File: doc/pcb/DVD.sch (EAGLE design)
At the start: 26 parts, among them IC1 7805, IC2 74HC14N

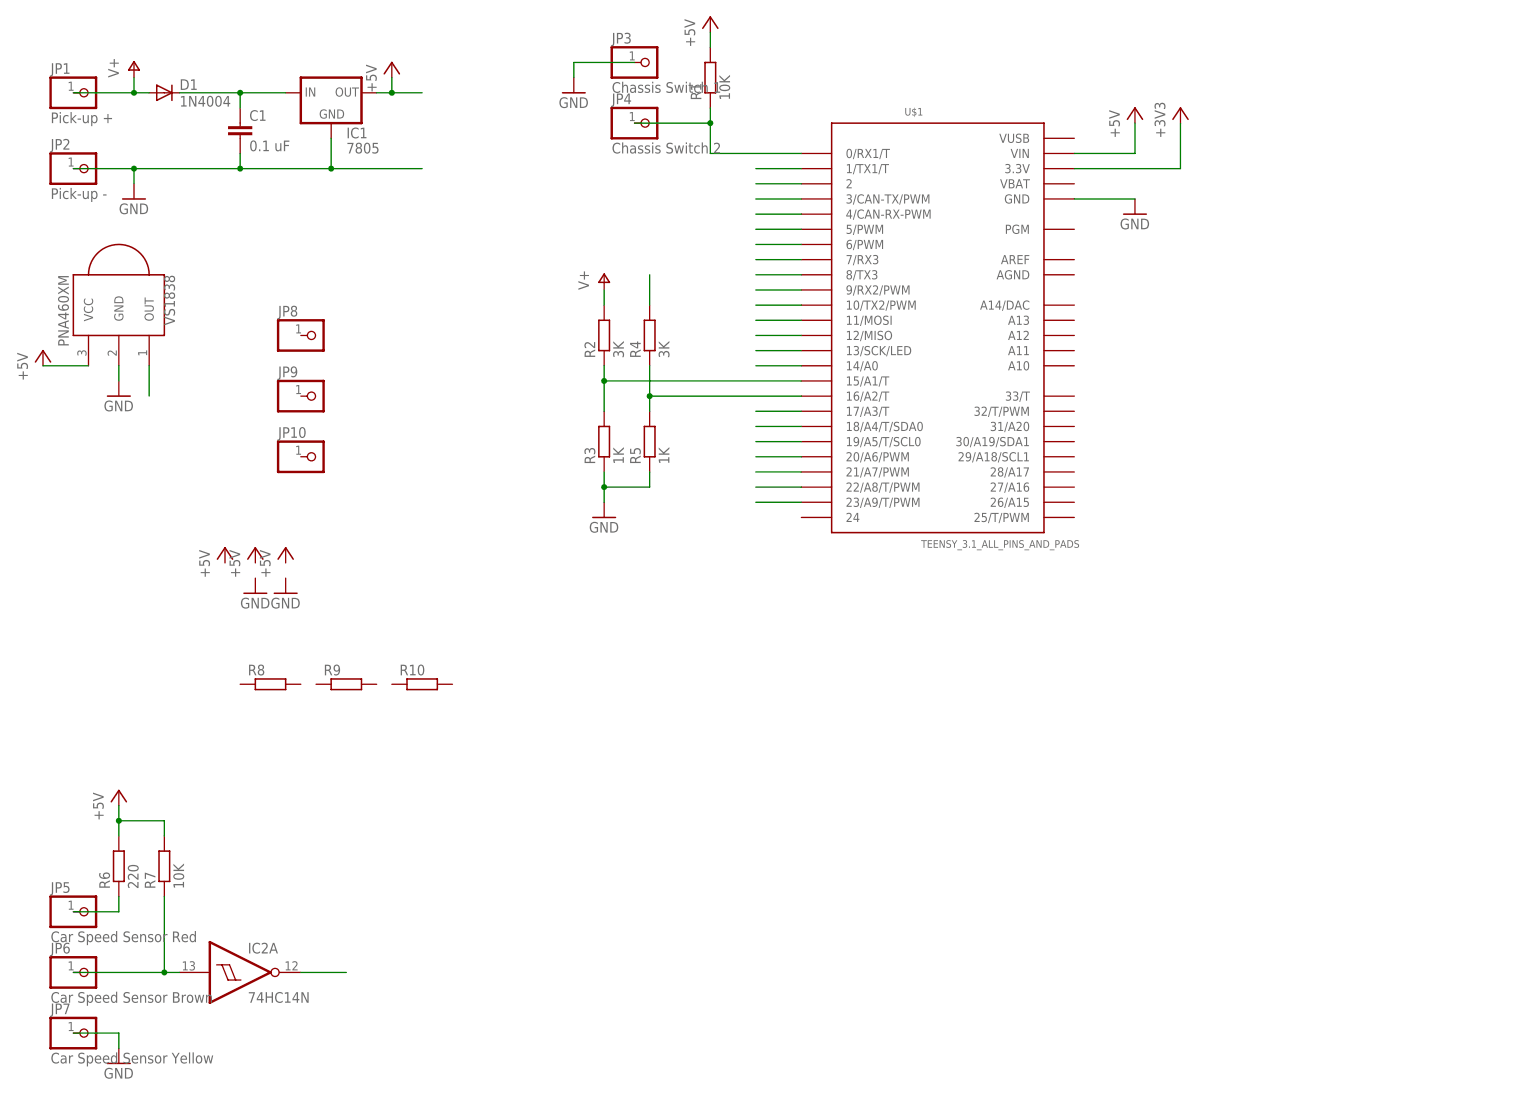
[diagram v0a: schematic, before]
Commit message: PCB Schematics update
Added all known components
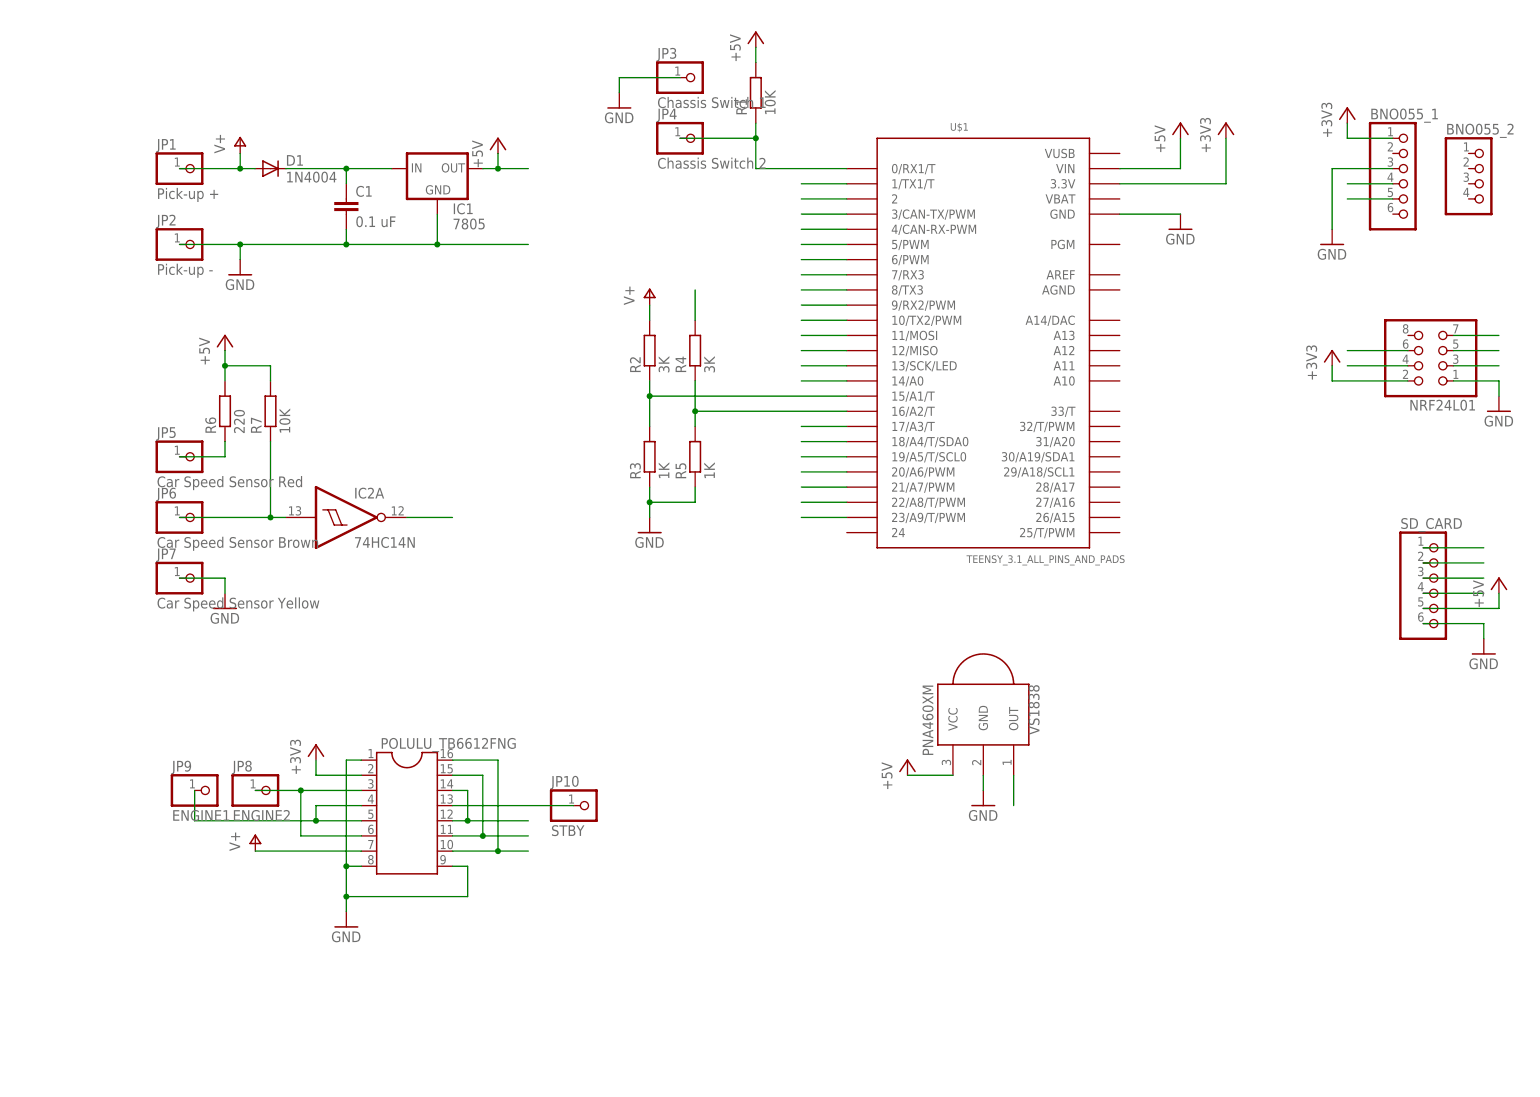
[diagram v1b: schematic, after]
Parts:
- removed R10, R8, R9: (no value), resistor:R-EU_0204/7
- added BNO055_1, SD_CARD: (no value), adafruit:PINHD-1X6
- added BNO055_2: (no value), pinhead:PINHD-1X4
- added NRF24L01: (no value), adafruit:PINHD-2X4
- added POLULU_TB6612FNG: (no value), ic-package:DIL16
- JP10: value (none) -> STBY
- JP8: value (none) -> ENGINE2
- JP9: value (none) -> ENGINE1
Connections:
- removed net N$12: U$1.18/A4/T/SDA0
- removed net N$13: U$1.19/A5/T/SCL0
- removed net N$14: U$1.21/A7/PWM
- removed net N$15: U$1.22/A8/T/PWM
- removed net N$16: U$1.23/A9/T/PWM
- removed net N$23: U$1.14/A0
- removed net N$5: U$1.9/RX2/PWM
- removed net N$6: U$1.10/TX2/PWM
- removed net N$7: U$1.11/MOSI
- removed net N$8: U$1.12/MISO
- new net CE: NRF24L01.3, U$1.8/TX3
- new net CSN_RADIO: NRF24L01.4, U$1.10/TX2/PWM
- new net CSN_SD: SD_CARD.1, U$1.9/RX2/PWM
- new net ENGINE1: JP9.1, POLULU_TB6612FNG.4, POLULU_TB6612FNG.5
- new net IN1: POLULU_TB6612FNG.12, POLULU_TB6612FNG.14, U$1.23/A9/T/PWM
- new net IN2: POLULU_TB6612FNG.11, POLULU_TB6612FNG.15, U$1.22/A8/T/PWM
- new net JP8: JP8.1, POLULU_TB6612FNG.3, POLULU_TB6612FNG.6
- new net MISO: NRF24L01.7, SD_CARD.4, U$1.12/MISO
- new net MOSI: NRF24L01.6, SD_CARD.3, U$1.11/MOSI
- new net PWM: POLULU_TB6612FNG.10, POLULU_TB6612FNG.16, U$1.21/A7/PWM
- new net SCK: NRF24L01.5, SD_CARD.2, U$1.14/A0
- new net SCL: BNO055_1.5, U$1.19/A5/T/SCL0
- new net SDA: BNO055_1.4, U$1.18/A4/T/SDA0
- net +3V3: now also BNO055_1.1, NRF24L01.2, POLULU_TB6612FNG.2
- net +5V: now also SD_CARD.5
- net GND: now also BNO055_1.3, NRF24L01.1, POLULU_TB6612FNG.1, POLULU_TB6612FNG.8, POLULU_TB6612FNG.9, SD_CARD.6
- net N$4: now also JP10.1, POLULU_TB6612FNG.13; no longer U$1.8/TX3
- net V+: now also POLULU_TB6612FNG.7
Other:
- moved on the sheet: C1, D1, IC1, IC2A, JP1, JP10, JP2, JP3, JP4, JP5, JP6, JP7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

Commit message: Updated PCB
Moved V+
Added Capacitors
Added power to schmitt trigger
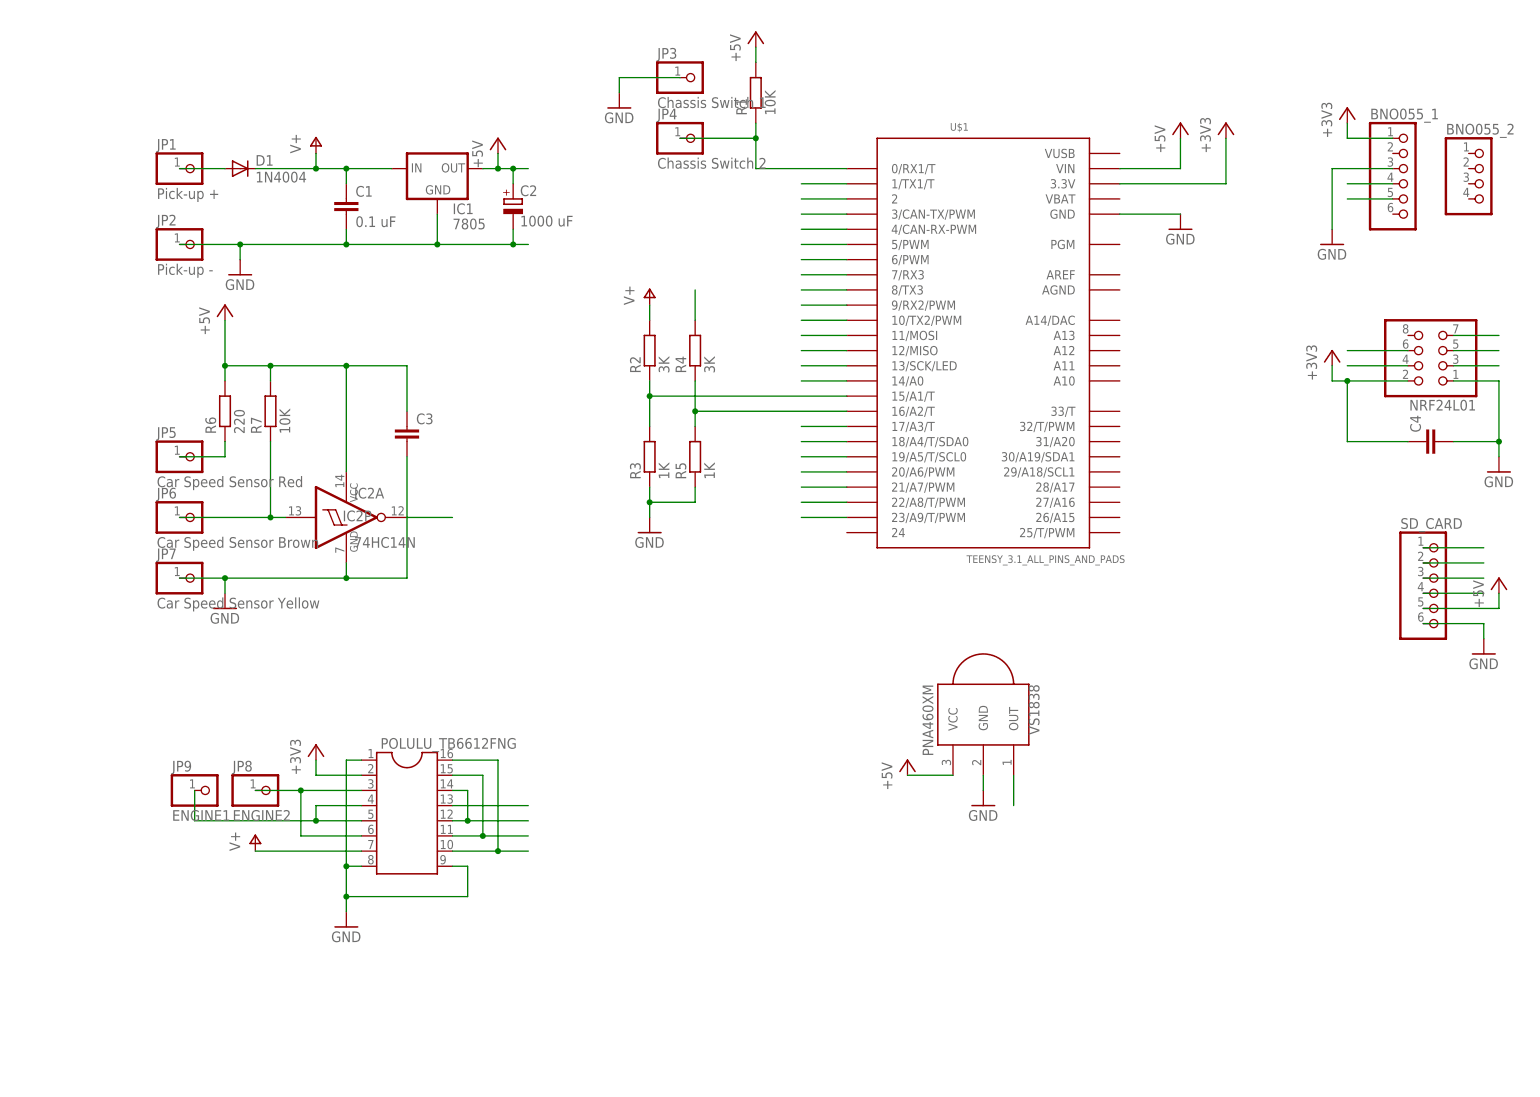
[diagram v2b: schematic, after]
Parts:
- removed JP10: STBY, pinhead:PINHD-1X1
- added C2: 1000 uF, resistor:CPOL-EUP128-50
- added C3, C4: (no value), resistor:C-EU025-025X050
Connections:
- removed net N$1: C1.1, D1.C, IC1.IN
- removed net N$25: U$1.20/A6/PWM
- removed net N$4: JP10.1, POLULU_TB6612FNG.13
- new net N$5: D1.A, JP1.1
- new net STBY: POLULU_TB6612FNG.13, U$1.20/A6/PWM
- net +3V3: now also C4.1
- net +5V: now also C2.+, C3.1, IC2P.VCC
- net GND: now also C2.-, C3.2, C4.2, IC2P.GND
- net V+: now also C1.1, D1.C, IC1.IN; no longer D1.A, JP1.1
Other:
- moved on the sheet: D1
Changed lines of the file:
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@@
 <part name="JP8" library="pinhead" deviceset="PINHD-1X1" device="" value="ENGINE2"/>
 <part name="JP9" library="pinhead" deviceset="PINHD-1X1" device="" value="ENGINE1"/>
-<part name="JP10" library="pinhead" deviceset="PINHD-1X1" device="" value="STBY"/>
 <part name="U$1" library="Teensy_3_Series_Board_v1.0" deviceset="TEENSY_3.1_ALL_PINS_AND_PADS" device=""/>
 <part name="VS1838" library="adafruit" deviceset="PNA460XM" device=""/>
@@
 <part name="POLULU_TB6612FNG" library="ic-package" deviceset="DIL16" device=""/>
 <part name="P+11" library="supply1" deviceset="V+" device=""/>
+<part name="C2" library="resistor" deviceset="CPOL-EU" device="P128-50" value="1000 uF"/>
+<part name="C3" library="resistor" deviceset="C-EU" device="025-025X050"/>
+<part name="C4" library="resistor" deviceset="C-EU" device="025-025X050"/>
 </parts>
 <sheets>
@@
 <instance part="FRAME1" gate="G$2" x="119.38" y="-12.7"/>
 <instance part="GND1" gate="1" x="-7.62" y="121.92"/>
-<instance part="P+1" gate="1" x="-7.62" y="144.78"/>
+<instance part="P+1" gate="1" x="5.08" y="144.78"/>
 <instance part="C1" gate="G$1" x="10.16" y="134.62"/>
 <instance part="IC1" gate="A" x="25.4" y="139.7"/>
 <instance part="JP1" gate="G$1" x="-15.24" y="139.7"/>
 <instance part="JP2" gate="G$1" x="-15.24" y="127"/>
-<instance part="D1" gate="1" x="-2.54" y="139.7"/>
+<instance part="D1" gate="1" x="-7.62" y="139.7"/>
 <instance part="P+2" gate="1" x="35.56" y="144.78"/>
 <instance part="P+3" gate="1" x="149.86" y="147.32"/>
@@
 <instance part="JP8" gate="G$1" x="-2.54" y="35.56"/>
 <instance part="JP9" gate="G$1" x="-12.7" y="35.56"/>
-<instance part="JP10" gate="G$1" x="50.8" y="33.02"/>
 <instance part="U$1" gate="G$1" x="116.84" y="111.76"/>
 <instance part="VS1838" gate="G$1" x="116.84" y="48.26" rot="R270"/>
 <instance part="P+4" gate="1" x="104.14" y="40.64"/>
-<instance part="P+5" gate="1" x="-10.16" y="111.76"/>
+<instance part="P+5" gate="1" x="-10.16" y="116.84"/>
 <instance part="P+6" gate="1" x="78.74" y="162.56"/>
 <instance part="P+8" gate="1" x="203.2" y="71.12"/>
@@
 <instance part="+3V3" gate="G$1" x="5.08" y="43.18"/>
 <instance part="+3V4" gate="G$1" x="177.8" y="149.86"/>
-<instance part="GND10" gate="1" x="203.2" y="99.06"/>
+<instance part="GND10" gate="1" x="203.2" y="88.9"/>
 <instance part="GND11" gate="1" x="10.16" y="12.7"/>
 <instance part="GND12" gate="1" x="175.26" y="127"/>
@@
 <instance part="POLULU_TB6612FNG" gate="G$1" x="20.32" y="33.02"/>
 <instance part="P+11" gate="1" x="-5.08" y="27.94"/>
+<instance part="IC2" gate="P" x="10.16" y="81.28"/>
+<instance part="C2" gate="G$1" x="38.1" y="134.62"/>
+<instance part="C3" gate="G$1" x="20.32" y="96.52"/>
+<instance part="C4" gate="G$1" x="190.5" y="93.98" rot="R90"/>
 </instances>
 <busses>
@@
 <net name="V+" class="0">
 <segment>
-<pinref part="P+1" gate="1" pin="V+"/>
-<wire x1="-17.78" y1="139.7" x2="-7.62" y2="139.7" width="0.1524" layer="91"/>
-<wire x1="-7.62" y1="142.24" x2="-7.62" y2="139.7" width="0.1524" layer="91"/>
-<pinref part="D1" gate="1" pin="A"/>
-<wire x1="-7.62" y1="139.7" x2="-5.08" y2="139.7" width="0.1524" layer="91"/>
-<junction x="-7.62" y="139.7"/>
-<pinref part="JP1" gate="G$1" pin="1"/>
-</segment>
-<segment>
 <pinref part="R2" gate="G$1" pin="2"/>
 <pinref part="P+10" gate="1" pin="V+"/>
@@
 <pinref part="P+11" gate="1" pin="V+"/>
 </segment>
-</net>
-<net name="N$1" class="0">
 <segment>
 <pinref part="D1" gate="1" pin="C"/>
 <pinref part="IC1" gate="A" pin="IN"/>
-<wire x1="0" y1="139.7" x2="10.16" y2="139.7" width="0.1524" layer="91"/>
+<wire x1="-5.08" y1="139.7" x2="5.08" y2="139.7" width="0.1524" layer="91"/>
+<wire x1="5.08" y1="139.7" x2="10.16" y2="139.7" width="0.1524" layer="91"/>
 <wire x1="17.78" y1="139.7" x2="10.16" y2="139.7" width="0.1524" layer="91"/>
 <pinref part="C1" gate="G$1" pin="1"/>
 <wire x1="10.16" y1="139.7" x2="10.16" y2="137.16" width="0.1524" layer="91"/>
 <junction x="10.16" y="139.7"/>
+<pinref part="P+1" gate="1" pin="V+"/>
+<wire x1="5.08" y1="142.24" x2="5.08" y2="139.7" width="0.1524" layer="91"/>
+<junction x="5.08" y="139.7"/>
 </segment>
 </net>
@@
 <wire x1="10.16" y1="127" x2="25.4" y2="127" width="0.1524" layer="91"/>
 <wire x1="25.4" y1="132.08" x2="25.4" y2="127" width="0.1524" layer="91"/>
-<wire x1="25.4" y1="127" x2="40.64" y2="127" width="0.1524" layer="91"/>
+<wire x1="25.4" y1="127" x2="38.1" y2="127" width="0.1524" layer="91"/>
 <junction x="-7.62" y="127"/>
 <junction x="10.16" y="127"/>
 <junction x="25.4" y="127"/>
 <pinref part="JP2" gate="G$1" pin="1"/>
+<wire x1="38.1" y1="127" x2="40.64" y2="127" width="0.1524" layer="91"/>
+<wire x1="38.1" y1="129.54" x2="38.1" y2="127" width="0.1524" layer="91"/>
+<junction x="38.1" y="127"/>
+<pinref part="C2" gate="G$1" pin="-"/>
 </segment>
 <segment>
@@
 <wire x1="-10.16" y1="71.12" x2="-17.78" y2="71.12" width="0.1524" layer="91"/>
 <pinref part="JP7" gate="G$1" pin="1"/>
+<pinref part="IC2" gate="P" pin="GND"/>
+<wire x1="10.16" y1="73.66" x2="10.16" y2="71.12" width="0.1524" layer="91"/>
+<wire x1="10.16" y1="71.12" x2="-10.16" y2="71.12" width="0.1524" layer="91"/>
+<junction x="-10.16" y="71.12"/>
+<pinref part="C3" gate="G$1" pin="2"/>
+<wire x1="20.32" y1="91.44" x2="20.32" y2="71.12" width="0.1524" layer="91"/>
+<wire x1="20.32" y1="71.12" x2="10.16" y2="71.12" width="0.1524" layer="91"/>
+<junction x="10.16" y="71.12"/>
 </segment>
 <segment>
@@
 <pinref part="NRF24L01" gate="A" pin="1"/>
 <wire x1="195.58" y1="104.14" x2="203.2" y2="104.14" width="0.1524" layer="91"/>
-<wire x1="203.2" y1="104.14" x2="203.2" y2="101.6" width="0.1524" layer="91"/>
+<wire x1="203.2" y1="104.14" x2="203.2" y2="93.98" width="0.1524" layer="91"/>
 <pinref part="GND10" gate="1" pin="GND"/>
+<pinref part="C4" gate="G$1" pin="2"/>
+<wire x1="203.2" y1="93.98" x2="203.2" y2="91.44" width="0.1524" layer="91"/>
+<wire x1="195.58" y1="93.98" x2="203.2" y2="93.98" width="0.1524" layer="91"/>
+<junction x="203.2" y="93.98"/>
 </segment>
 <segment>
@@
 <pinref part="P+2" gate="1" pin="+5V"/>
 <wire x1="35.56" y1="142.24" x2="35.56" y2="139.7" width="0.1524" layer="91"/>
-<wire x1="35.56" y1="139.7" x2="40.64" y2="139.7" width="0.1524" layer="91"/>
+<wire x1="35.56" y1="139.7" x2="38.1" y2="139.7" width="0.1524" layer="91"/>
 <junction x="35.56" y="139.7"/>
+<wire x1="38.1" y1="139.7" x2="40.64" y2="139.7" width="0.1524" layer="91"/>
+<wire x1="38.1" y1="137.16" x2="38.1" y2="139.7" width="0.1524" layer="91"/>
+<junction x="38.1" y="139.7"/>
+<pinref part="C2" gate="G$1" pin="+"/>
 </segment>
 <segment>
@@
 <pinref part="P+5" gate="1" pin="+5V"/>
 <pinref part="R6" gate="G$1" pin="2"/>
-<wire x1="-10.16" y1="109.22" x2="-10.16" y2="106.68" width="0.1524" layer="91"/>
+<wire x1="-10.16" y1="114.3" x2="-10.16" y2="106.68" width="0.1524" layer="91"/>
 <wire x1="-10.16" y1="104.14" x2="-10.16" y2="106.68" width="0.1524" layer="91"/>
 <wire x1="-10.16" y1="106.68" x2="-2.54" y2="106.68" width="0.1524" layer="91"/>
@@
 <wire x1="-2.54" y1="106.68" x2="-2.54" y2="104.14" width="0.1524" layer="91"/>
 <junction x="-10.16" y="106.68"/>
+<pinref part="IC2" gate="P" pin="VCC"/>
+<wire x1="10.16" y1="88.9" x2="10.16" y2="106.68" width="0.1524" layer="91"/>
+<wire x1="10.16" y1="106.68" x2="-2.54" y2="106.68" width="0.1524" layer="91"/>
+<junction x="-2.54" y="106.68"/>
+<pinref part="C3" gate="G$1" pin="1"/>
+<wire x1="20.32" y1="99.06" x2="20.32" y2="106.68" width="0.1524" layer="91"/>
+<wire x1="20.32" y1="106.68" x2="10.16" y2="106.68" width="0.1524" layer="91"/>
+<junction x="10.16" y="106.68"/>
 </segment>
 <segment>
@@
 </segment>
 </net>
-<net name="N$25" class="0">
+<net name="STBY" class="0">
 <segment>
 <pinref part="U$1" gate="G$1" pin="20/A6/PWM"/>
 <wire x1="93.98" y1="88.9" x2="86.36" y2="88.9" width="0.1524" layer="91"/>
+</segment>
+<segment>
+<pinref part="POLULU_TB6612FNG" gate="G$1" pin="13"/>
+<wire x1="27.94" y1="33.02" x2="40.64" y2="33.02" width="0.1524" layer="91"/>
 </segment>
 </net>
@@
 <segment>
 <pinref part="NRF24L01" gate="A" pin="2"/>
-<wire x1="187.96" y1="104.14" x2="175.26" y2="104.14" width="0.1524" layer="91"/>
+<wire x1="187.96" y1="104.14" x2="177.8" y2="104.14" width="0.1524" layer="91"/>
+<wire x1="177.8" y1="104.14" x2="175.26" y2="104.14" width="0.1524" layer="91"/>
 <wire x1="175.26" y1="104.14" x2="175.26" y2="106.68" width="0.1524" layer="91"/>
 <pinref part="+3V2" gate="G$1" pin="+3V3"/>
+<pinref part="C4" gate="G$1" pin="1"/>
+<wire x1="187.96" y1="93.98" x2="177.8" y2="93.98" width="0.1524" layer="91"/>
+<wire x1="177.8" y1="93.98" x2="177.8" y2="104.14" width="0.1524" layer="91"/>
+<junction x="177.8" y="104.14"/>
 </segment>
 <segment>
@@
 </segment>
 </net>
-<net name="N$4" class="0">
-<segment>
-<pinref part="POLULU_TB6612FNG" gate="G$1" pin="13"/>
-<pinref part="JP10" gate="G$1" pin="1"/>
-<wire x1="27.94" y1="33.02" x2="48.26" y2="33.02" width="0.1524" layer="91"/>
-</segment>
-</net>
+<net name="N$5" class="0">
+<segment>
+<wire x1="-17.78" y1="139.7" x2="-10.16" y2="139.7" width="0.1524" layer="91"/>
+<pinref part="D1" gate="1" pin="A"/>
+<pinref part="JP1" gate="G$1" pin="1"/>
+</segment>
+</net>
